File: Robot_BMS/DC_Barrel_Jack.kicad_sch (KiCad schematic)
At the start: 1 part, among them J2 DCJ200-10-A-XX-K_REVA

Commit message: ex charging circuit last appearence
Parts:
- removed J2: DCJ200-10-A-XX-K_REVA, DCJ200-10-A-XX-K_REVA:GCT_DCJ200-10-A-XX-K_REVA, symbol DC Barrel Jack:DCJ200-10-A-XX-K_REVA
- added J4: 694108301002, 694108301002, symbol 694108301002:694108301002
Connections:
- net GND: now also J4.2, J4.3
- new net DC_BARREL_JACK: J4.1
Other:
- note added: "30V 5A MAX 2.5mm inner diameter"
- note added: "DC BARREL JACK Connector"
- note added: "This gets fed directly into the 13V charging IC"
- note removed: "DC BARREL JACK POWER SUPPLY"
- note removed: "DC Barrel Jack gets fed into Sepic converter"
- note removed: "SW REG takes in 9-24V from DC barrel jack design uses TI Webench designer but datasheet also referenced when layout was done."
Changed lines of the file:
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@@
 	(generator_version "8.0")
 	(paper "A4")
-	(wire
-		(pts
-			(xy 215.646 73.406) (xy 195.58 73.406)
-		)
-		(stroke
-			(width 0)
-			(type default)
-		)
-	)
-	(wire
-		(pts
-			(xy 215.646 78.486) (xy 212.852 78.486)
-		)
-		(stroke
-			(width 0)
-			(type default)
-		)
-	)
-	(wire
-		(pts
-			(xy 212.852 78.486) (xy 212.852 78.74)
-		)
-		(stroke
-			(width 0)
-			(type default)
-		)
-	)
-	(text "SW REG takes in 9-24V from DC barrel jack\ndesign uses TI Webench designer but\ndatasheet also referenced when layout\nwas done."
-		(exclude_from_sim no)
-		(at 227.33 148.844 0)
+	(junction
+		(at 134.62 103.124)
+		(diameter 0)
+		(color 0 0 0 0)
+	)
+	(wire
+		(pts
+			(xy 154.94 103.124) (xy 154.94 99.314)
+		)
+		(stroke
+			(width 0)
+			(type default)
+		)
+	)
+	(wire
+		(pts
+			(xy 134.62 103.124) (xy 134.62 108.966)
+		)
+		(stroke
+			(width 0)
+			(type default)
+		)
+	)
+	(wire
+		(pts
+			(xy 154.94 105.664) (xy 175.006 105.664)
+		)
+		(stroke
+			(width 0)
+			(type default)
+		)
+	)
+	(wire
+		(pts
+			(xy 154.94 99.314) (xy 134.62 99.314)
+		)
+		(stroke
+			(width 0)
+			(type default)
+		)
+	)
+	(wire
+		(pts
+			(xy 134.62 99.314) (xy 134.62 103.124)
+		)
+		(stroke
+			(width 0)
+			(type default)
+		)
+	)
+	(text "This gets fed directly into the 13V charging IC"
+		(exclude_from_sim no)
+		(at 108.966 39.624 0)
+		(effects
+			(font
+				(size 5.08 5.08)
+			)
+		)
+	)
+	(text "30V 5A MAX\n2.5mm inner diameter"
+		(exclude_from_sim no)
+		(at 146.304 119.126 0)
+		(effects
+			(font
+				(size 1.905 1.905)
+			)
+		)
+	)
+	(text "DC Barrel Jack connector\n"
+		(exclude_from_sim no)
+		(at 148.336 89.916 0)
 		(effects
 			(font
@@
 		)
 	)
-	(text "DC Barrel Jack connector\n"
-		(exclude_from_sim no)
-		(at 220.98 64.262 0)
-		(effects
-			(font
-				(size 2.54 2.54)
-			)
-		)
-	)
-	(text "DC BARREL JACK POWER SUPPLY"
-		(exclude_from_sim no)
-		(at 109.22 20.066 0)
+	(text "DC BARREL JACK Connector\n"
+		(exclude_from_sim no)
+		(at 93.98 23.622 0)
 		(effects
 			(font
@@
 		)
 	)
-	(text "DC Barrel Jack gets fed into Sepic converter\n\n"
-		(exclude_from_sim no)
-		(at 163.576 76.2 0)
+	(hierarchical_label "DC_BARREL_JACK"
+		(shape output)
+		(at 175.006 105.664 0)
 		(effects
 			(font
 				(size 1.27 1.27)
 			)
-		)
-	)
-	(label "DC_BARREL_SUPPLY"
-		(at 195.58 73.406 0)
-		(effects
-			(font
-				(size 1.27 1.27)
-			)
-			(justify left bottom)
-		)
-	)
-	(symbol
-		(lib_id "DC Barrel Jack:DCJ200-10-A-XX-K_REVA")
-		(at 220.726 75.946 0)
-		(mirror y)
-		(unit 1)
-		(exclude_from_sim no)
-		(in_bom yes)
-		(on_board yes)
-		(dnp no)
-		(property "Reference" "J2"
-			(at 223.9617 66.04 0)
-			(effects
-				(font
-					(size 1.27 1.27)
-				)
-			)
-		)
-		(property "Value" "DCJ200-10-A-XX-K_REVA"
-			(at 223.9617 68.58 0)
-			(effects
-				(font
-					(size 1.27 1.27)
-				)
-			)
-		)
-		(property "Footprint" "DCJ200-10-A-XX-K_REVA:GCT_DCJ200-10-A-XX-K_REVA"
-			(at 220.726 75.946 0)
-			(effects
-				(font
-					(size 1.27 1.27)
-				)
-				(justify bottom)
-				(hide yes)
-			)
-		)
-		(property "Datasheet" ""
-			(at 220.726 75.946 0)
-			(effects
-				(font
-					(size 1.27 1.27)
-				)
-				(hide yes)
-			)
-		)
-		(property "Description" ""
-			(at 220.726 75.946 0)
-			(effects
-				(font
-					(size 1.27 1.27)
-				)
-				(hide yes)
-			)
-		)
-		(property "PARTREV" "A"
-			(at 220.726 75.946 0)
-			(effects
-				(font
-					(size 1.27 1.27)
-				)
-				(justify bottom)
-				(hide yes)
-			)
-		)
-		(property "STANDARD" "Manufacturer Recommendations"
-			(at 220.726 75.946 0)
-			(effects
-				(font
-					(size 1.27 1.27)
-				)
-				(justify bottom)
-				(hide yes)
-			)
-		)
-		(property "SNAPEDA_PN" "DCJ200-10-A-K1-K"
-			(at 220.726 75.946 0)
-			(effects
-				(font
-					(size 1.27 1.27)
-				)
-				(justify bottom)
-				(hide yes)
-			)
-		)
-		(property "MAXIMUM_PACKAGE_HEIGHT" "11 mm"
-			(at 220.726 75.946 0)
-			(effects
-				(font
-					(size 1.27 1.27)
-				)
-				(justify bottom)
-				(hide yes)
-			)
-		)
-		(property "MANUFACTURER" "Global Connector Technology"
-			(at 220.726 75.946 0)
-			(effects
-				(font
-					(size 1.27 1.27)
-				)
-				(justify bottom)
-				(hide yes)
-			)
-		)
-		(pin "1"
-		)
-		(pin "3"
-		)
-		(pin "2"
-		)
-		(instances
-			(project ""
-				(path "/72551b1c-3d40-4199-8911-e5b015f4abec/7a60a594-7330-4ecb-a3c9-8c0f96aa21b4"
-					(reference "J2")
-					(unit 1)
-				)
-			)
+			(justify left)
 		)
 	)
 	(symbol
 		(lib_id "power:GND")
-		(at 212.852 78.74 0)
+		(at 134.62 108.966 0)
 		(mirror y)
 		(unit 1)
@@
 		(dnp no)
 		(fields_autoplaced yes)
-		(property "Reference" "#PWR025"
-			(at 212.852 85.09 0)
+		(property "Reference" "#PWR026"
+			(at 134.62 115.316 0)
 			(effects
 				(font
@@
 		)
 		(property "Value" "GND"
-			(at 212.852 83.82 0)
+			(at 134.62 114.046 0)
 			(effects
 				(font
@@
 		)
 		(property "Footprint" ""
-			(at 212.852 78.74 0)
+			(at 134.62 108.966 0)
 			(effects
 				(font
@@
 		)
 		(property "Datasheet" ""
-			(at 212.852 78.74 0)
+			(at 134.62 108.966 0)
 			(effects
 				(font
@@
 		)
 		(property "Description" "Power symbol creates a global label with name \"GND\" , ground"
-			(at 212.852 78.74 0)
+			(at 134.62 108.966 0)
 			(effects
 				(font
@@
 		)
 		(pin "1"
+		)
+		(instances
+			(project "Robot_BMS"
+				(path "/72551b1c-3d40-4199-8911-e5b015f4abec/7a60a594-7330-4ecb-a3c9-8c0f96aa21b4"
+					(reference "#PWR026")
+					(unit 1)
+				)
+			)
+		)
+	)
+	(symbol
+		(lib_id "694108301002:694108301002")
+		(at 134.62 103.124 0)
+		(unit 1)
+		(exclude_from_sim no)
+		(in_bom yes)
+		(on_board yes)
+		(dnp no)
+		(property "Reference" "J4"
+			(at 144.78 93.472 0)
+			(effects
+				(font
+					(size 1.27 1.27)
+				)
+			)
+		)
+		(property "Value" "694108301002"
+			(at 144.78 96.012 0)
+			(effects
+				(font
+					(size 1.27 1.27)
+				)
+			)
+		)
+		(property "Footprint" "694108301002"
+			(at 151.13 198.044 0)
+			(effects
+				(font
+					(size 1.27 1.27)
+				)
+				(justify left top)
+				(hide yes)
+			)
+		)
+		(property "Datasheet" "https://www.we-online.com/components/products/datasheet/6941xx301002.pdf"
+			(at 151.13 298.044 0)
+			(effects
+				(font
+					(size 1.27 1.27)
+				)
+				(justify left top)
+				(hide yes)
+			)
+		)
+		(property "Description" "DC Power Jack Right Angled 5A, 30 V(DC), Contact Resistance 50 m"
+			(at 134.62 103.124 0)
+			(effects
+				(font
+					(size 1.27 1.27)
+				)
+				(hide yes)
+			)
+		)
+		(property "Height" "11"
+			(at 151.13 498.044 0)
+			(effects
+				(font
+					(size 1.27 1.27)
+				)
+				(justify left top)
+				(hide yes)
+			)
+		)
+		(property "Mouser Part Number" "710-694108301002"
+			(at 151.13 598.044 0)
+			(effects
+				(font
+					(size 1.27 1.27)
+				)
+				(justify left top)
+				(hide yes)
+			)
+		)
+		(property "Mouser Price/Stock" "https://www.mouser.co.uk/ProductDetail/Wurth-Elektronik/694108301002?qs=a9WhcLg8qCwpBR6w1flhOw%3D%3D"
+			(at 151.13 698.044 0)
+			(effects
+				(font
+					(size 1.27 1.27)
+				)
+				(justify left top)
+				(hide yes)
+			)
+		)
+		(property "Manufacturer_Name" "Wurth Elektronik"
+			(at 151.13 798.044 0)
+			(effects
+				(font
+					(size 1.27 1.27)
+				)
+				(justify left top)
+				(hide yes)
+			)
+		)
+		(property "Manufacturer_Part_Number" "694108301002"
+			(at 151.13 898.044 0)
+			(effects
+				(font
+					(size 1.27 1.27)
+				)
+				(justify left top)
+				(hide yes)
+			)
+		)
+		(pin "2"
+		)
+		(pin "1"
+		)
+		(pin "3"
 		)
 		(instances
 			(project ""
 				(path "/72551b1c-3d40-4199-8911-e5b015f4abec/7a60a594-7330-4ecb-a3c9-8c0f96aa21b4"
-					(reference "#PWR025")
+					(reference "J4")
 					(unit 1)
 				)

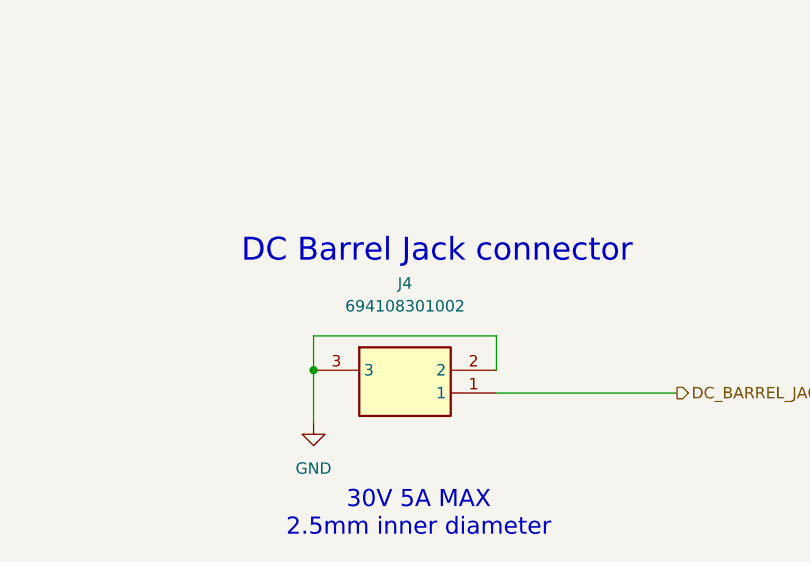
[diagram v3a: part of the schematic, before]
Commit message: System drawing down on top schematic, will start inputting footprints
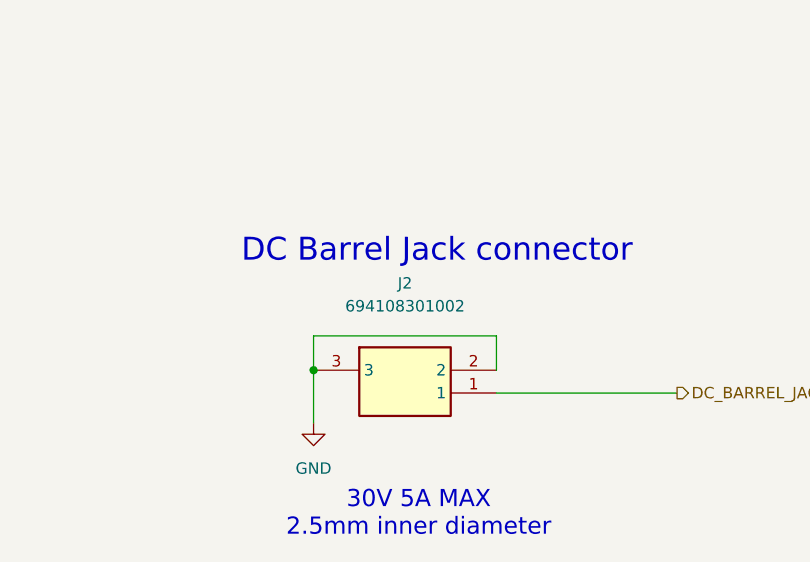
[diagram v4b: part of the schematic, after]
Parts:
- renumbered J4 to J2
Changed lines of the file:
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@@
 		(dnp no)
 		(fields_autoplaced yes)
-		(property "Reference" "#PWR026"
+		(property "Reference" "#PWR029"
 			(at 134.62 115.316 0)
 			(effects
@@
 			(project "Robot_BMS"
 				(path "/72551b1c-3d40-4199-8911-e5b015f4abec/7a60a594-7330-4ecb-a3c9-8c0f96aa21b4"
-					(reference "#PWR026")
+					(reference "#PWR029")
 					(unit 1)
 				)
@@
 		(on_board yes)
 		(dnp no)
-		(property "Reference" "J4"
+		(property "Reference" "J2"
 			(at 144.78 93.472 0)
 			(effects
@@
 			(project ""
 				(path "/72551b1c-3d40-4199-8911-e5b015f4abec/7a60a594-7330-4ecb-a3c9-8c0f96aa21b4"
-					(reference "J4")
+					(reference "J2")
 					(unit 1)
 				)

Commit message: adding footprints and actual passive components
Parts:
- J3: renamed from J2; footprint 694108301002 -> RobotBMS:694108301002
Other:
- note added: "All standard Passive componenets are 0603 imperial"
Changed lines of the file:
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@@
+		)
+	)
+	(text "All standard Passive\ncomponenets are 0603 imperial"
+		(exclude_from_sim no)
+		(at 228.6 173.736 0)
+		(effects
+			(font
+				(size 2.54 2.54)
+			)
 		)
 	)
@@
 		(on_board yes)
 		(dnp no)
-		(property "Reference" "J2"
+		(property "Reference" "J3"
 			(at 144.78 93.472 0)
 			(effects
@@
 			)
 		)
-		(property "Footprint" "694108301002"
+		(property "Footprint" "RobotBMS:694108301002"
 			(at 151.13 198.044 0)
 			(effects
@@
 			(project ""
 				(path "/72551b1c-3d40-4199-8911-e5b015f4abec/7a60a594-7330-4ecb-a3c9-8c0f96aa21b4"
-					(reference "J2")
+					(reference "J3")
 					(unit 1)
 				)

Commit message: BOM done, with total price £40
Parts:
- J3: Price (none) -> 0.804
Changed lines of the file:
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@@
 			)
 		)
-		(property "Datasheet" "https://www.we-online.com/components/products/datasheet/6941xx301002.pdf"
+		(property "Datasheet" "https://www.mouser.co.uk/ProductDetail/Wurth-Elektronik/694108301002?qs=a9WhcLg8qCwpBR6w1flhOw%3D%3D&srsltid=AfmBOoprH2athC-B50XwA6svXtxN7ZZwMgzBne9QUqA8l4yvF5rTB4wq"
 			(at 151.13 298.044 0)
 			(effects
@@
 				(hide yes)
 			)
+		)
+		(property "Price" "0.804"
+			(at 134.62 103.124 0)
+			(effects
+				(font
+					(size 1.27 1.27)
+				)
+				(hide yes)
+			)

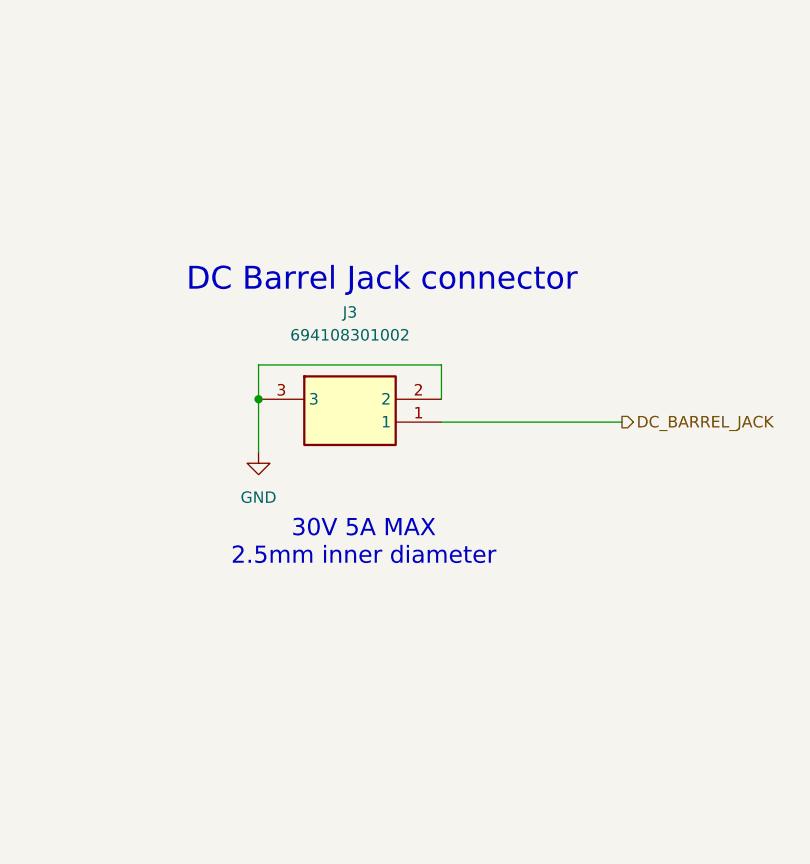
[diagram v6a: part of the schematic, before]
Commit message: switching usb c pd chip to ap33772 due to better support online
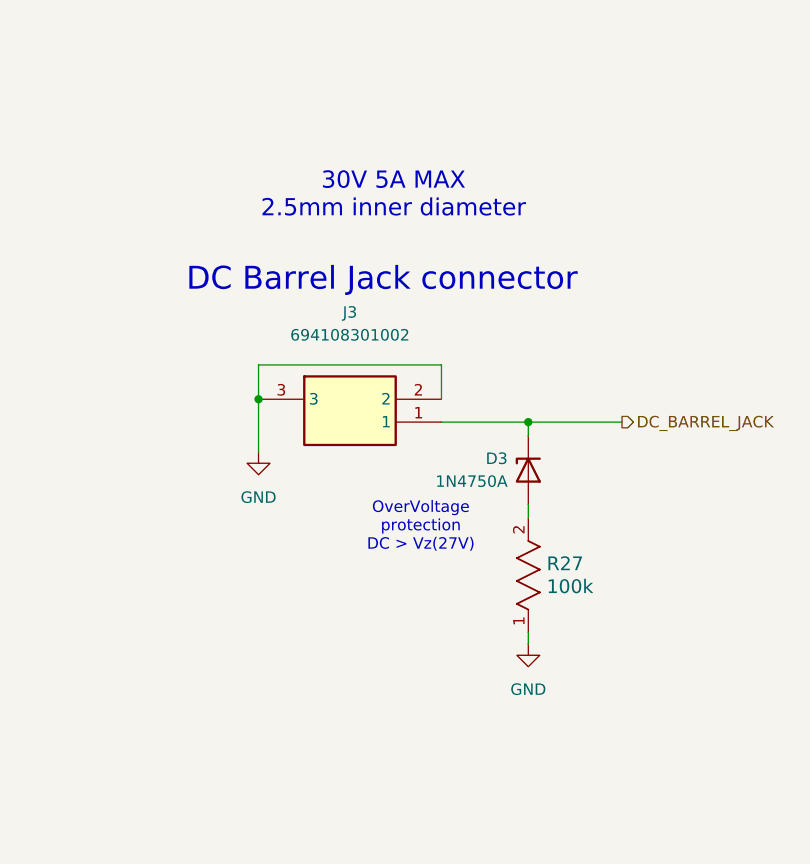
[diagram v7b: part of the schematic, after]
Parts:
- added D3: 1N4750A, Diode_THT:D_DO-41_SOD81_P10.16mm_Horizontal, symbol Diode:1N47xxA
- added R27: 100k, RobotBMS:RES_R0603_ROM, symbol ESR03EZPF1003:ESR03EZPF1003
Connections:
- net DC_BARREL_JACK: now also D3.1 (K)
- net GND: now also R27.1
- new net: D3.2 (A), R27.2
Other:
- note added: "OverVoltage protection DC > Vz(27V)"

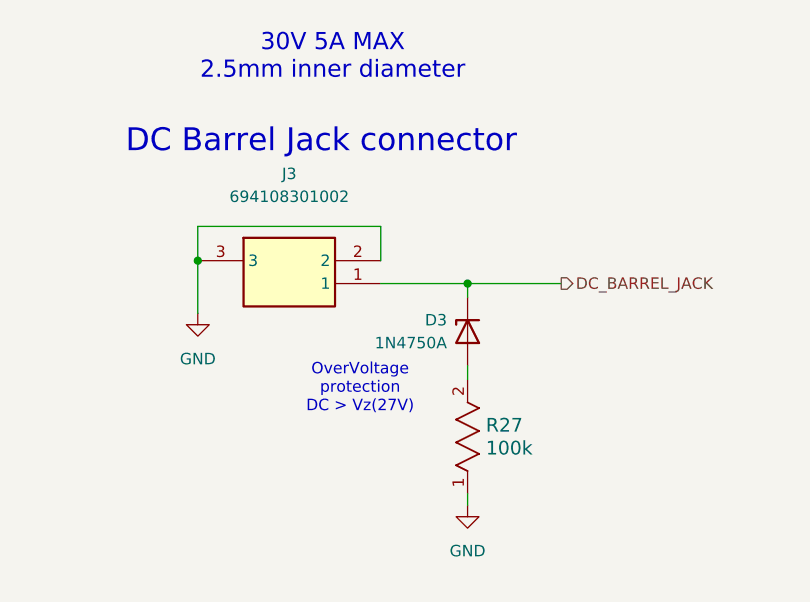
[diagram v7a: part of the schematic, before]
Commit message: placed connectors for BMS PCB
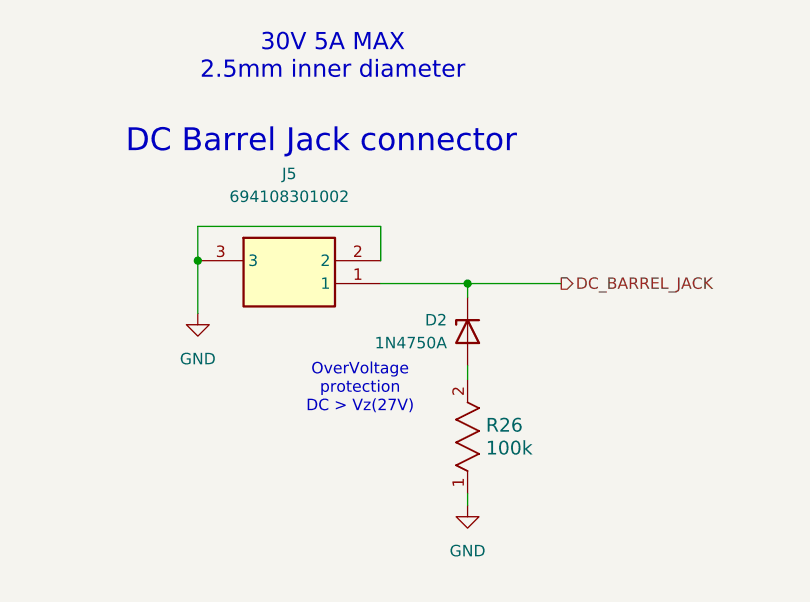
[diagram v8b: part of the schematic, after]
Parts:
- renumbered D3 to D2, J3 to J5, R27 to R26
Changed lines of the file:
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@@
 		(dnp no)
 		(fields_autoplaced yes)
-		(property "Reference" "#PWR040"
+		(property "Reference" "#PWR037"
 			(at 164.592 136.652 0)
 			(effects
@@
 			(project "Robot_BMS"
 				(path "/72551b1c-3d40-4199-8911-e5b015f4abec/7a60a594-7330-4ecb-a3c9-8c0f96aa21b4"
-					(reference "#PWR040")
+					(reference "#PWR037")
 					(unit 1)
 				)
@@
 		(dnp no)
 		(fields_autoplaced yes)
-		(property "Reference" "#PWR029"
+		(property "Reference" "#PWR036"
 			(at 134.62 115.316 0)
 			(effects
@@
 			(project "Robot_BMS"
 				(path "/72551b1c-3d40-4199-8911-e5b015f4abec/7a60a594-7330-4ecb-a3c9-8c0f96aa21b4"
-					(reference "#PWR029")
+					(reference "#PWR036")
 					(unit 1)
 				)
@@
 		(on_board yes)
 		(dnp no)
-		(property "Reference" "J3"
+		(property "Reference" "J5"
 			(at 144.78 93.472 0)
 			(effects
@@
 			(project ""
 				(path "/72551b1c-3d40-4199-8911-e5b015f4abec/7a60a594-7330-4ecb-a3c9-8c0f96aa21b4"
-					(reference "J3")
+					(reference "J5")
 					(unit 1)
 				)
@@
 		(on_board yes)
 		(dnp no)
-		(property "Reference" "D3"
+		(property "Reference" "D2"
 			(at 162.306 109.7279 90)
 			(effects
@@
 			(project "Robot_BMS"
 				(path "/72551b1c-3d40-4199-8911-e5b015f4abec/7a60a594-7330-4ecb-a3c9-8c0f96aa21b4"
-					(reference "D3")
+					(reference "D2")
 					(unit 1)
 				)
@@
 		(dnp no)
 		(fields_autoplaced yes)
-		(property "Reference" "R27"
+		(property "Reference" "R26"
 			(at 166.624 121.4119 90)
 			(effects
@@
 			(project "Robot_BMS"
 				(path "/72551b1c-3d40-4199-8911-e5b015f4abec/7a60a594-7330-4ecb-a3c9-8c0f96aa21b4"
-					(reference "R27")
+					(reference "R26")
 					(unit 1)
 				)
